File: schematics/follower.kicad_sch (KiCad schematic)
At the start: 26 parts, among them M2 Motor, M3 Motor, Q1 TLE5206_2S, Q2 TLE5206_2S, SW5 Reset, U10 PIC32MX170F256B, U5 Tape_Left, U6 Tape_Middle, U7 Tape_Right, U8 Quadrature_Encoder, U9 Quadrature_Encoder

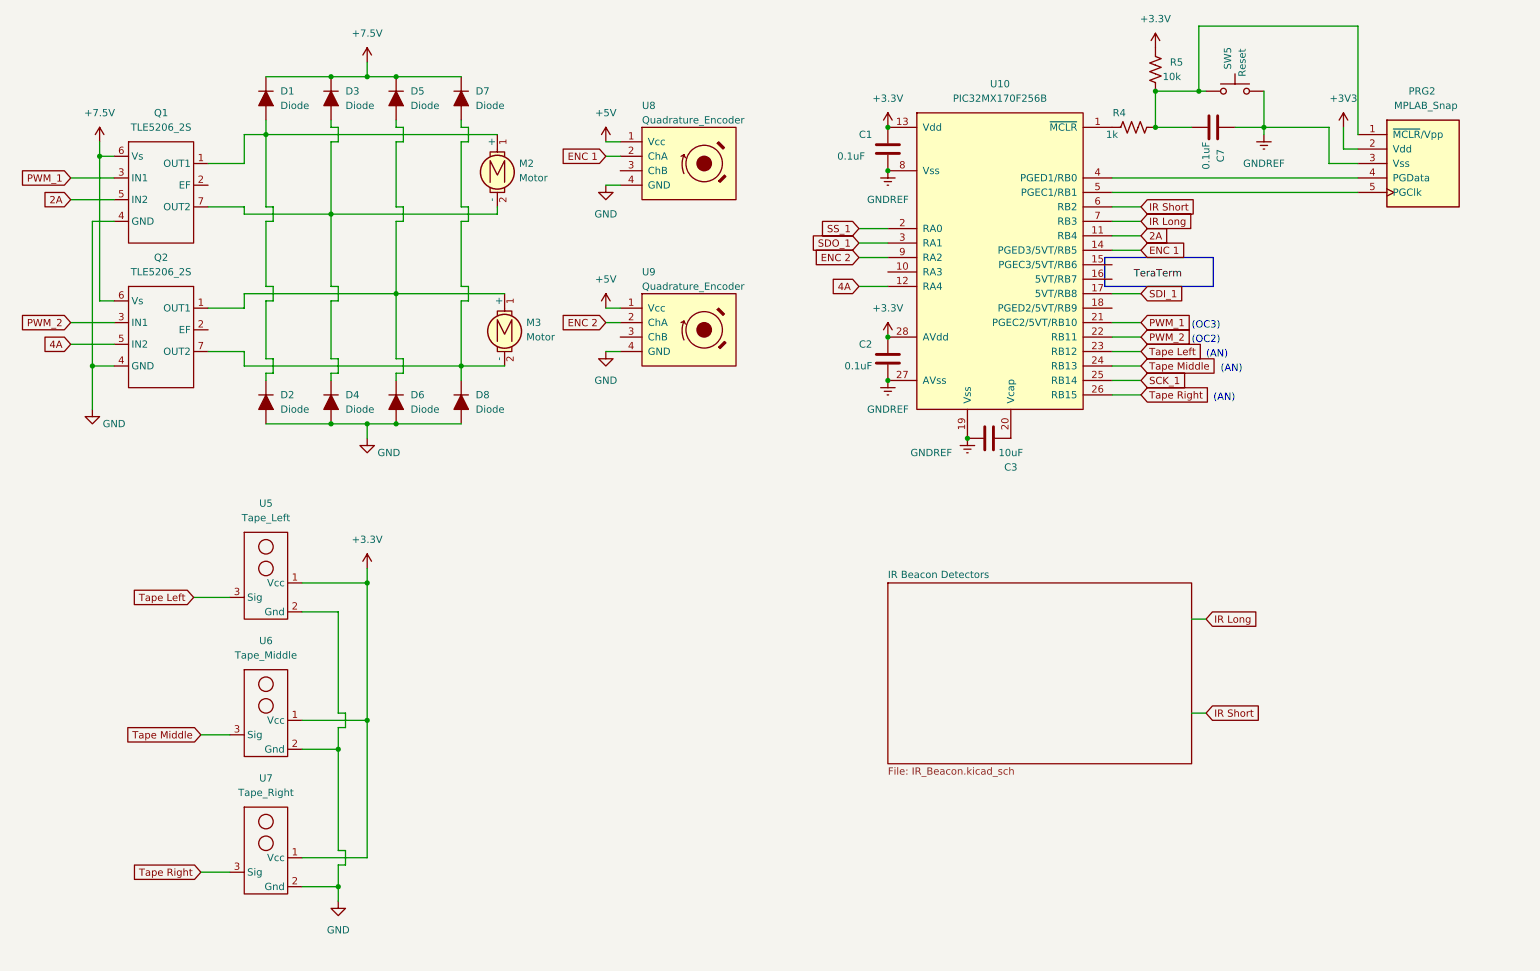
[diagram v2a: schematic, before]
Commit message: Adjust left and right motors with button presses.
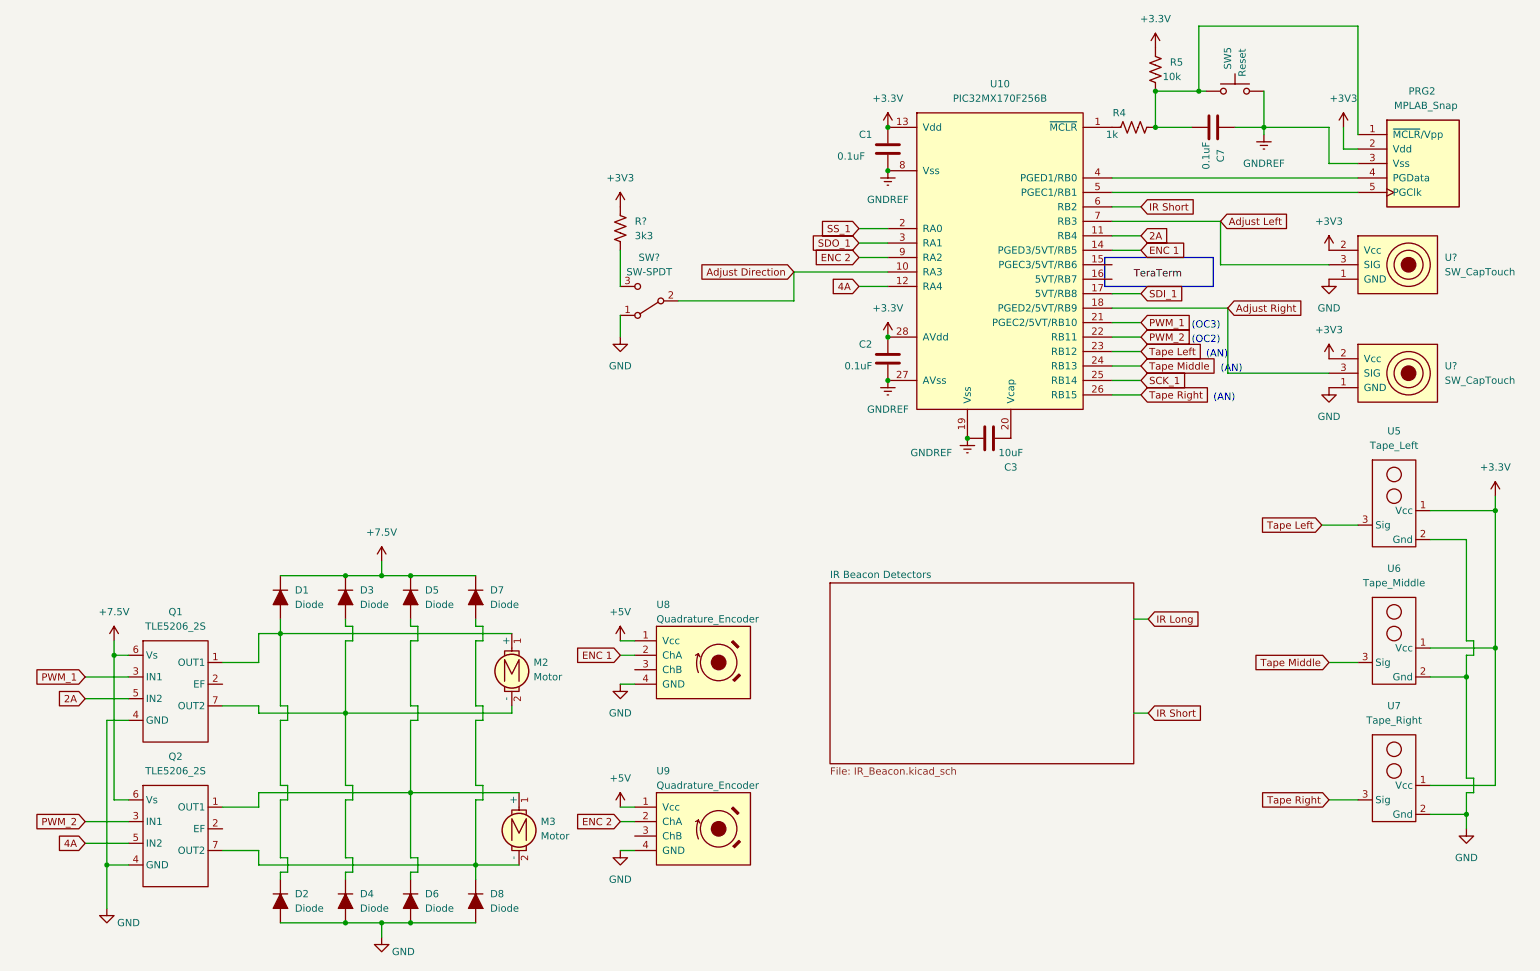
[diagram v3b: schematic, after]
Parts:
- added R?: 3k3, symbol 218 spdl:Res1
- added SW?: SW-SPDT, symbol 218 spdl:SW-SPDT
- added U? (x2): SW_CapTouch, symbol 218 spdl:SW_CapTouch
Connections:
- net +3V3: now also R?.1, U?.2 (Vcc), U?.2 (Vcc)
- net GND: now also SW?.1 (A), U?.1 (GND), U?.1 (GND)
- net IR Long: no longer U10.7 (RB3)
- net Adjust Direction: now reaches U10.10 (RA3)
- net Adjust Direction: now also SW?.2 (B)
- net Adjust Right: now reaches U10.18 (PGED2/5VT/RB9)
- net Adjust Right: now also U?.3 (SIG)
- new net: R?.2, SW?.3 (C)
- new net Adjust Left: U10.7 (RB3), U?.3 (SIG)
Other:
- moved on the sheet: D1, D2, D3, D4, D5, D6, D7, D8, M2, M3, Q1, Q2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

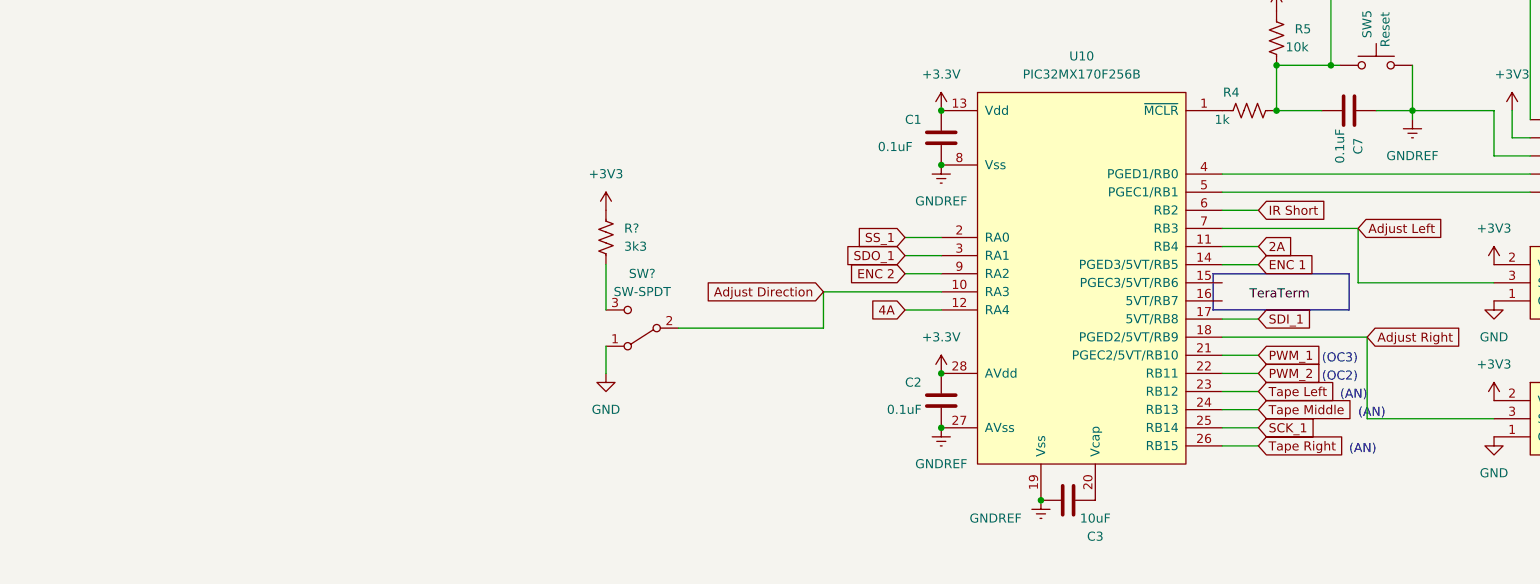
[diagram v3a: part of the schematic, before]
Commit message: Update kicad schematic and comment out Test Harness prints.
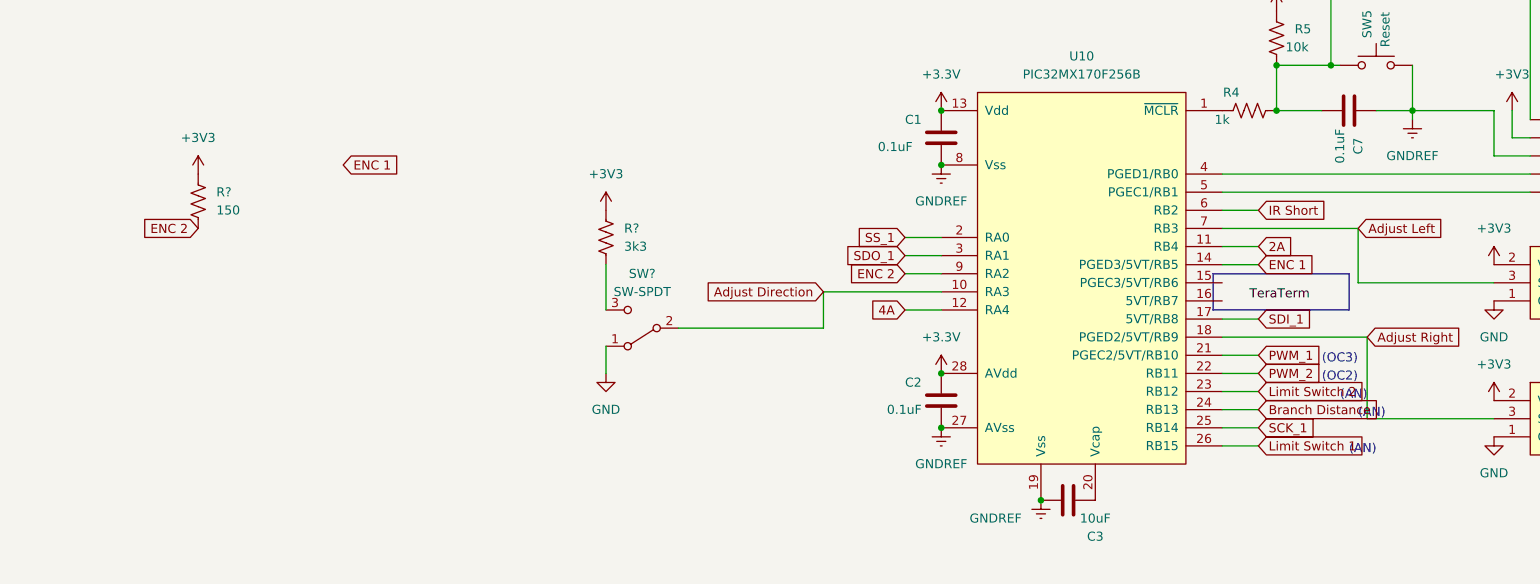
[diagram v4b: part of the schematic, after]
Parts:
- added R?: 150, symbol 218 spdl:Res1
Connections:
- net +3V3: now also R?.1
- net ENC 2: now also R?.2
- net Tape Left: no longer U10.23 (RB12)
- net Tape Middle: no longer U10.24 (RB13)
- net Tape Right: no longer U10.26 (RB15)
- new net Branch Distance: U10.24 (RB13)
- new net Limit Switch 1: U10.26 (RB15)
- new net Limit Switch 2: U10.23 (RB12)
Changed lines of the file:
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@@
     )
   )
-  (global_label "Tape Left" (shape input) (at 217.17 74.93 0) (fields_autoplaced)
-    (effects (font (size 1.27 1.27)) (justify left))
-    (property "Intersheet References" "${INTERSHEET_REFS}" (id 0) (at 228.4731 74.8506 0)
-      (effects (font (size 1.27 1.27)) (justify left) hide)
-    )
-  )
-  (global_label "Tape Middle" (shape input) (at 217.17 77.47 0) (fields_autoplaced)
-    (effects (font (size 1.27 1.27)) (justify left))
-    (property "Intersheet References" "${INTERSHEET_REFS}" (id 0) (at 231.0131 77.3906 0)
+  (global_label "Limit Switch 2" (shape input) (at 217.17 74.93 0) (fields_autoplaced)
+    (effects (font (size 1.27 1.27)) (justify left))
+    (property "Intersheet References" "${INTERSHEET_REFS}" (id 0) (at 233.4926 74.8506 0)
+      (effects (font (size 1.27 1.27)) (justify left) hide)
+    )
+  )
+  (global_label "Branch Distance" (shape input) (at 217.17 77.47 0) (fields_autoplaced)
+    (effects (font (size 1.27 1.27)) (justify left))
+    (property "Intersheet References" "${INTERSHEET_REFS}" (id 0) (at 235.2464 77.3906 0)
       (effects (font (size 1.27 1.27)) (justify left) hide)
     )
@@
     )
   )
+  (global_label "ENC 2" (shape input) (at 68.58 52.07 180) (fields_autoplaced)
+    (effects (font (size 1.27 1.27)) (justify right))
+    (property "Intersheet References" "${INTERSHEET_REFS}" (id 0) (at 60.2402 51.9906 0)
+      (effects (font (size 1.27 1.27)) (justify right) hide)
+    )
+  )
   (global_label "4A" (shape input) (at 31.75 161.29 180) (fields_autoplaced)
     (effects (font (size 1.27 1.27)) (justify right))
@@
     )
   )
-  (global_label "Tape Right" (shape input) (at 217.17 82.55 0) (fields_autoplaced)
-    (effects (font (size 1.27 1.27)) (justify left))
-    (property "Intersheet References" "${INTERSHEET_REFS}" (id 0) (at 229.8036 82.4706 0)
+  (global_label "Limit Switch 1" (shape input) (at 217.17 82.55 0) (fields_autoplaced)
+    (effects (font (size 1.27 1.27)) (justify left))
+    (property "Intersheet References" "${INTERSHEET_REFS}" (id 0) (at 233.4926 82.4706 0)
+      (effects (font (size 1.27 1.27)) (justify left) hide)
+    )
+  )
+  (global_label "ENC 1" (shape input) (at 88.9 43.18 0) (fields_autoplaced)
+    (effects (font (size 1.27 1.27)) (justify left))
+    (property "Intersheet References" "${INTERSHEET_REFS}" (id 0) (at 97.2398 43.2594 0)
       (effects (font (size 1.27 1.27)) (justify left) hide)
     )
@@
     )
     (property "Datasheet" "" (id 3) (at 172.72 35.56 0)
+      (effects (font (size 1.27 1.27)) hide)
+    )
+    (pin "1")
+  )
+  (symbol (lib_id "power:+3V3") (at 68.58 44.45 0) (unit 1)
+    (in_bom yes) (on_board yes) (fields_autoplaced)
+    (property "Reference" "#PWR?" (id 0) (at 68.58 48.26 0)
+      (effects (font (size 1.27 1.27)) hide)
+    )
+    (property "Value" "+3V3" (id 1) (at 68.58 39.37 0))
+    (property "Footprint" "" (id 2) (at 68.58 44.45 0)
+      (effects (font (size 1.27 1.27)) hide)
+    )
+    (property "Datasheet" "" (id 3) (at 68.58 44.45 0)
       (effects (font (size 1.27 1.27)) hide)
     )
@@
     (pin "1")
   )
+  (symbol (lib_id "218 spdl:Res1") (at 68.58 48.26 0) (unit 1)
+    (in_bom yes) (on_board yes) (fields_autoplaced)
+    (property "Reference" "R?" (id 0) (at 71.12 46.9899 0)
+      (effects (font (size 1.27 1.27)) (justify left))
+    )
+    (property "Value" "150" (id 1) (at 71.12 49.5299 0)
+      (effects (font (size 1.27 1.27)) (justify left))
+    )
+    (property "Footprint" "" (id 2) (at 69.596 48.514 90)
+      (effects (font (size 1.27 1.27)) hide)
+    )
+    (property "Datasheet" "" (id 3) (at 68.58 48.26 0)
+      (effects (font (size 1.27 1.27)) hide)
+    )
+    (pin "1")
+    (pin "2")
+  )
   (symbol (lib_id "218 spdl:Diode") (at 100.33 118.11 270) (unit 1)
